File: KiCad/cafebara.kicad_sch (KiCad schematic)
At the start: 38 parts, among them J1 Micro_SD_Card_Det2, J2 USB_C_Receptacle_USB2.0_14P, J3 PROG, J4 Conn_01x19_MountingPin, J6 EDID, Q1 NMOS, SW1 SW_Push, U3 ATtiny1616-M, U4 M24C02-RMC

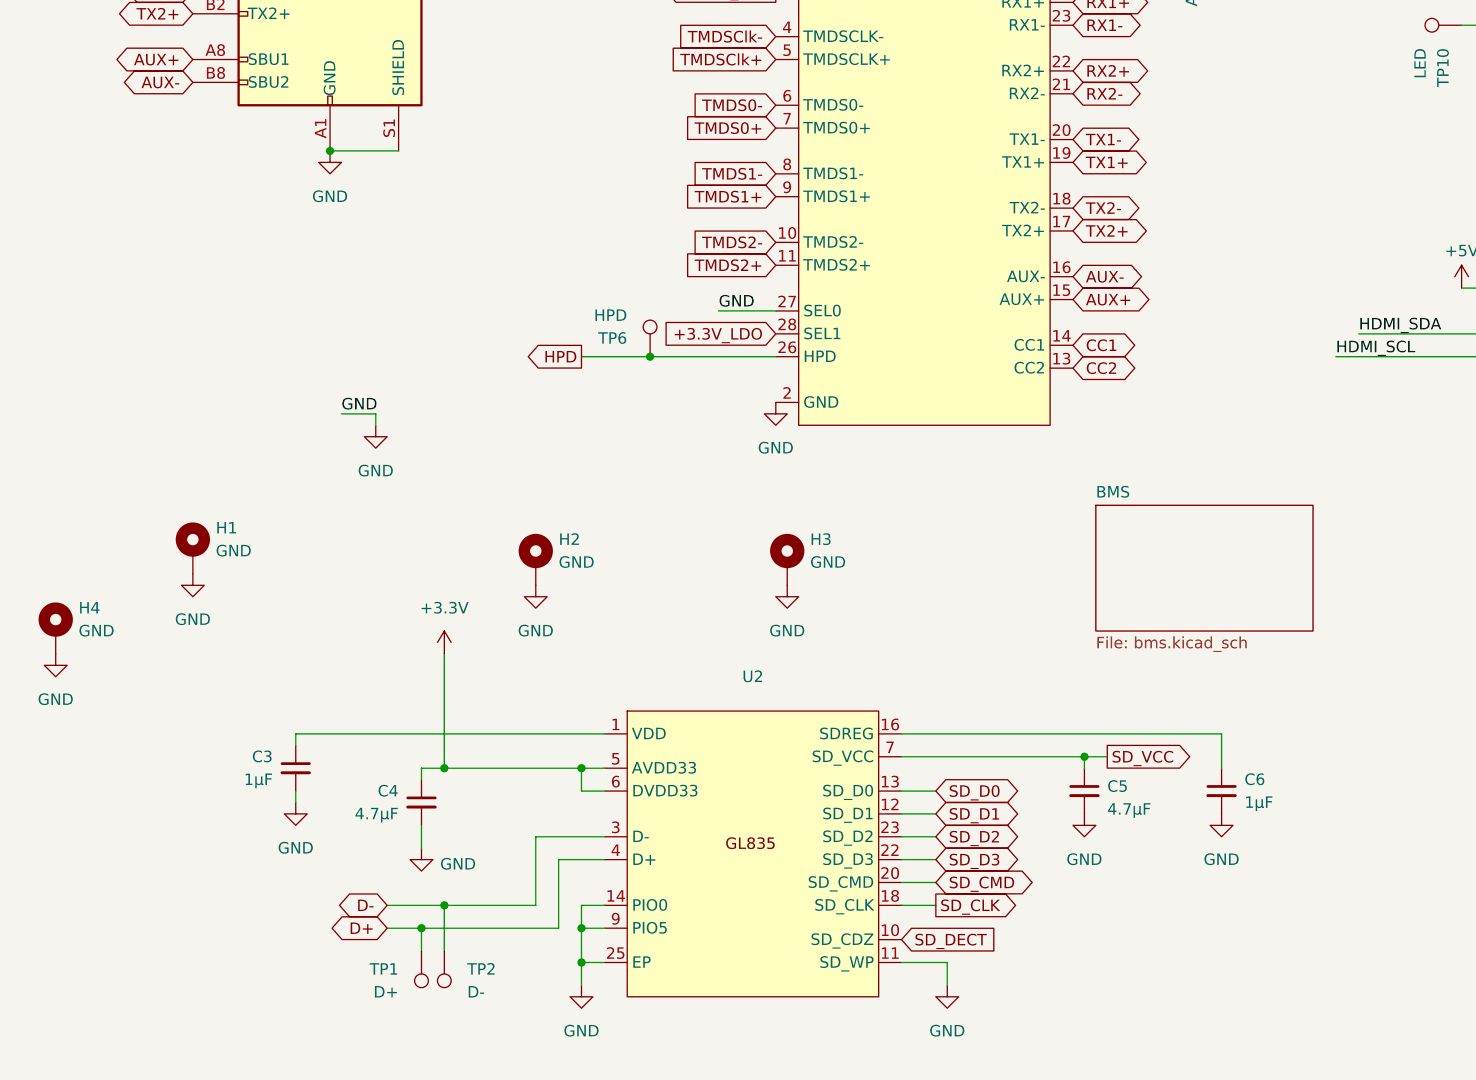
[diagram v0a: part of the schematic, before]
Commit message: Move to using 100W-Charging-PCB for battery charge
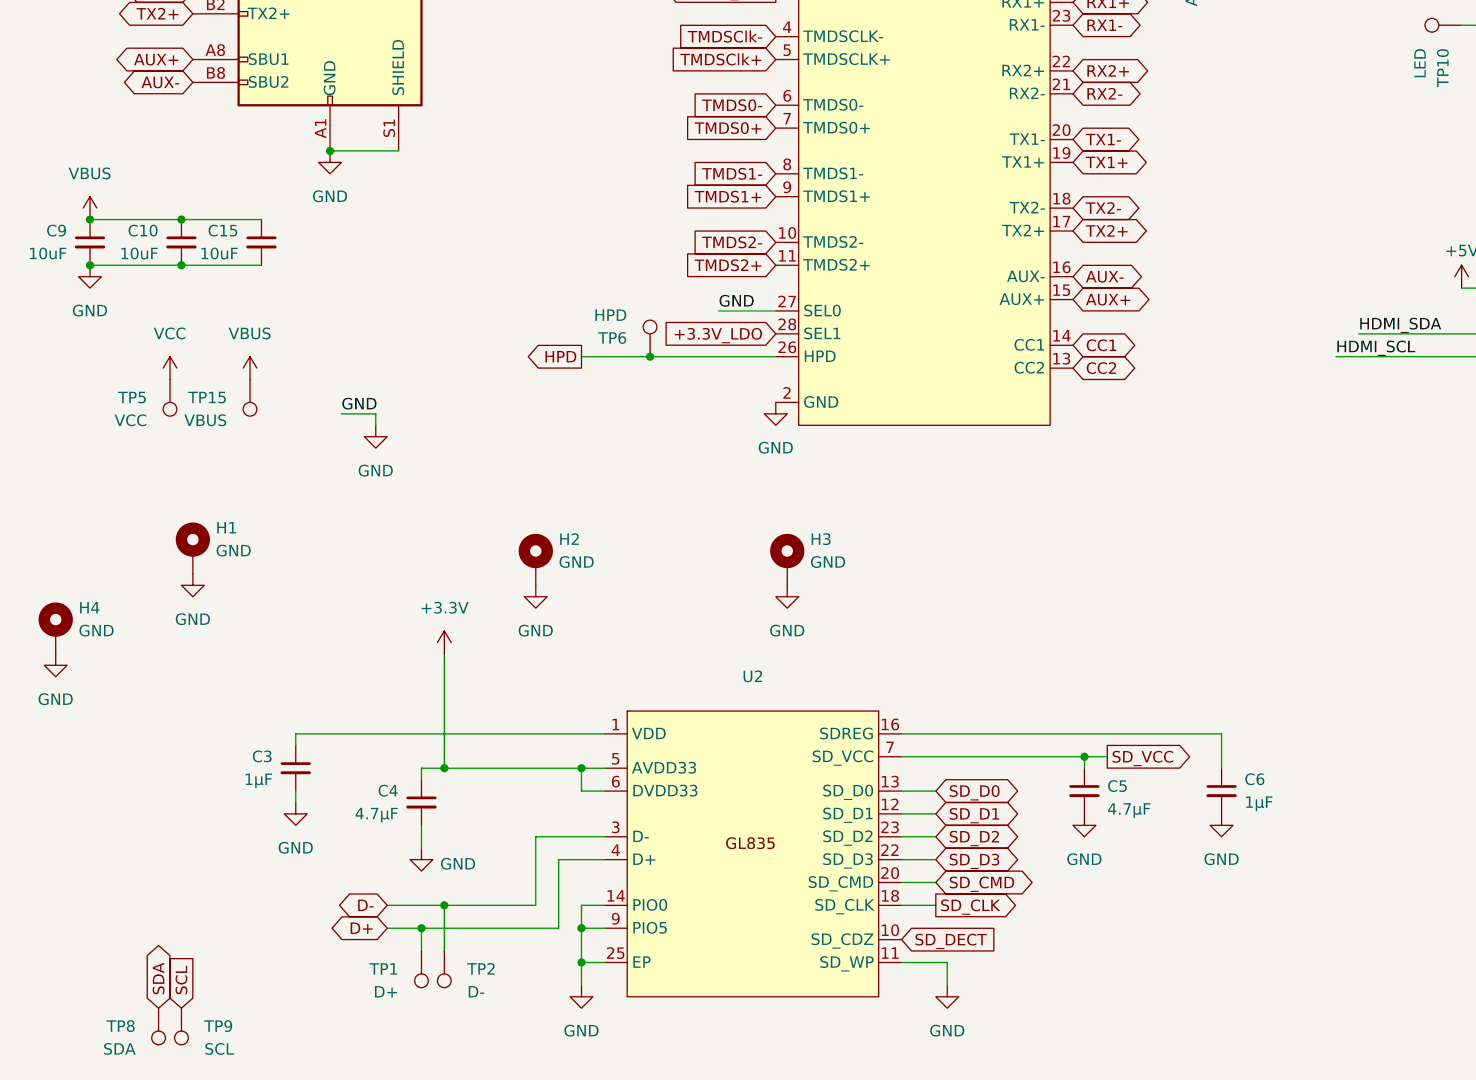
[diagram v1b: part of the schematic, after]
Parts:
- added C10, C15, C9: 10uF, Capacitor_SMD:C_0603_1608Metric, symbol Device:C_Small
- added TP15: VBUS, TestPoint:TestPoint_Plated_Hole_D2.0mm, symbol Connector:TestPoint
- added TP5: VCC, TestPoint:TestPoint_Plated_Hole_D2.0mm, symbol Connector:TestPoint
- added TP8: SDA, cafebara:TestPoint_Hole_D1.5mm_Small, symbol Connector:TestPoint
- added TP9: SCL, cafebara:TestPoint_Hole_D1.5mm_Small, symbol Connector:TestPoint
- TP1, TP2: footprint cafebara:TestPoint_Pad_D1.0mm_Small -> cafebara:TestPoint_Hole_D1.5mm_Small
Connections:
- net GND: now also C10.2, C15.2, C9.2
- net SCL: now also TP9.1
- net SDA: now also TP8.1
- net VBUS: now also C10.1, C15.1, C9.1, TP15.1
- net VCC: now also TP5.1
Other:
- removed sheet BMS

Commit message: misc changes and improvements
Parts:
- added TP12: ~{SHIP}, cafebara:TestPoint_Pad_D1.0mm_Small, symbol Connector:TestPoint
- J6: value EDID -> EDID_PRG
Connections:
- net ~{SHIP}: now reaches U3.15 (PC0)
- net ~{SHIP}: now also TP12.1
- no-connect marks 13 -> 12
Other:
- moved on the sheet: TP6
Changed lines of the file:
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@@
 	)
 	(junction
-		(at 85.09 110.49)
-		(diameter 0)
-		(color 0 0 0 0)
-	)
-	(junction
 		(at 77.47 173.99)
 		(diameter 0)
@@
 	)
 	(junction
+		(at 83.82 110.49)
+		(diameter 0)
+		(color 0 0 0 0)
+	)
+	(junction
 		(at 236.22 53.34)
 		(diameter 0)
@@
 	)
 	(no_connect
-		(at 217.17 50.8)
-	)
-	(no_connect
 		(at 186.69 68.58)
 	)
@@
 	)
 	(no_connect
-		(at 186.69 66.04)
-	)
-	(no_connect
 		(at 34.29 36.83)
 	)
@@
 	)
 	(no_connect
+		(at 217.17 50.8)
+	)
+	(no_connect
 		(at 217.17 60.96)
 	)
@@
 	(wire
 		(pts
+			(xy 267.97 107.95) (xy 273.05 107.95)
+		)
+		(stroke
+			(width 0)
+			(type default)
+		)
+	)
+	(wire
+		(pts
 			(xy 199.39 135.89) (xy 194.31 135.89)
 		)
@@
 	(wire
 		(pts
-			(xy 85.09 110.49) (xy 99.06 110.49)
-		)
-		(stroke
-			(width 0)
-			(type default)
-		)
-	)
-	(wire
-		(pts
 			(xy 54.61 116.84) (xy 54.61 118.11)
 		)
@@
 	(wire
 		(pts
-			(xy 77.47 110.49) (xy 85.09 110.49)
+			(xy 77.47 110.49) (xy 83.82 110.49)
 		)
 		(stroke
@@
 	(wire
 		(pts
+			(xy 83.82 110.49) (xy 99.06 110.49)
+		)
+		(stroke
+			(width 0)
+			(type default)
+		)
+	)
+	(wire
+		(pts
 			(xy 199.39 138.43) (xy 191.77 138.43)
 		)
@@
 		)
 	)
+	(global_label "~{SHIP}"
+		(shape output)
+		(at 186.69 66.04 180)
+		(fields_autoplaced yes)
+		(effects
+			(font
+				(size 1.27 1.27)
+			)
+			(justify right)
+		)
+		(property "Intersheetrefs" "${INTERSHEET_REFS}"
+			(at 179.29 66.04 0)
+			(effects
+				(font
+					(size 1.27 1.27)
+				)
+				(justify right)
+				(hide yes)
+			)
+		)
+	)
 	(global_label "TMDSClk+"
 		(shape output)
@@
 		)
 	)
+	(global_label "~{SHIP}"
+		(shape input)
+		(at 273.05 107.95 0)
+		(fields_autoplaced yes)
+		(effects
+			(font
+				(size 1.27 1.27)
+			)
+			(justify left)
+		)
+		(property "Intersheetrefs" "${INTERSHEET_REFS}"
+			(at 280.45 107.95 0)
+			(effects
+				(font
+					(size 1.27 1.27)
+				)
+				(justify left)
+				(hide yes)
+			)
+		)
+	)
 	(global_label "TMDS1+"
 		(shape output)
@@
 	(symbol
 		(lib_id "Connector:TestPoint")
-		(at 85.09 110.49 0)
+		(at 83.82 110.49 0)
 		(unit 1)
 		(exclude_from_sim no)
@@
 		(dnp no)
 		(property "Reference" "TP6"
-			(at 82.55 108.4581 0)
+			(at 81.28 108.4581 0)
 			(effects
 				(font
@@
 		)
 		(property "Value" "HPD"
-			(at 82.55 105.9181 0)
+			(at 81.28 105.9181 0)
 			(effects
 				(font
@@
 		)
 		(property "Footprint" "TestPoint:TestPoint_Pad_D1.5mm"
-			(at 90.17 110.49 0)
+			(at 88.9 110.49 0)
 			(effects
 				(font
@@
 		)
 		(property "Datasheet" "~"
-			(at 90.17 110.49 0)
+			(at 88.9 110.49 0)
 			(effects
 				(font
@@
 		)
 		(property "Description" "test point"
-			(at 85.09 110.49 0)
+			(at 83.82 110.49 0)
 			(effects
 				(font
@@
 			)
 		)
-		(property "Value" "EDID"
+		(property "Value" "EDID_PRG"
 			(at 173.99 40.6399 0)
 			(effects
@@
 					(unit 1)
 				)
+			)
+		)
+	)
+	(symbol
+		(lib_id "Connector:TestPoint")
+		(at 267.97 107.95 0)
+		(unit 1)
+		(exclude_from_sim no)
+		(in_bom yes)
+		(on_board yes)
+		(dnp no)
+		(property "Reference" "TP12"
+			(at 265.43 105.9181 0)
+			(effects
+				(font
+					(size 1.27 1.27)
+				)
+				(justify right)
+			)
+		)
+		(property "Value" "~{SHIP}"
+			(at 265.43 103.3781 0)
+			(effects
+				(font
+					(size 1.27 1.27)
+				)
+				(justify right)
+			)
+		)
+		(property "Footprint" "cafebara:TestPoint_Pad_D1.0mm_Small"
+			(at 273.05 107.95 0)
+			(effects
+				(font
+					(size 1.27 1.27)
+				)
+				(hide yes)
+			)
+		)
+		(property "Datasheet" "~"
+			(at 273.05 107.95 0)
+			(effects
+				(font
+					(size 1.27 1.27)
+				)
+				(hide yes)
+			)
+		)
+		(property "Description" "test point"
+			(at 267.97 107.95 0)
+			(effects
+				(font
+					(size 1.27 1.27)
+				)
+				(hide yes)
+			)
+		)
+		(pin "1"
+		)
+		(instances
+			(project "cafebara"
+				(path "/dcc89f95-4ae4-4756-aa81-33bf4d3c86ca"
+					(reference "TP12")
+					(unit 1)
+				)
